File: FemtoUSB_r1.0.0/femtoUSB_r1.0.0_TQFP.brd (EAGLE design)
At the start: 20.7 x 15.2 mm, 25 parts, among them IC1 ATSAMD21E18A-AU

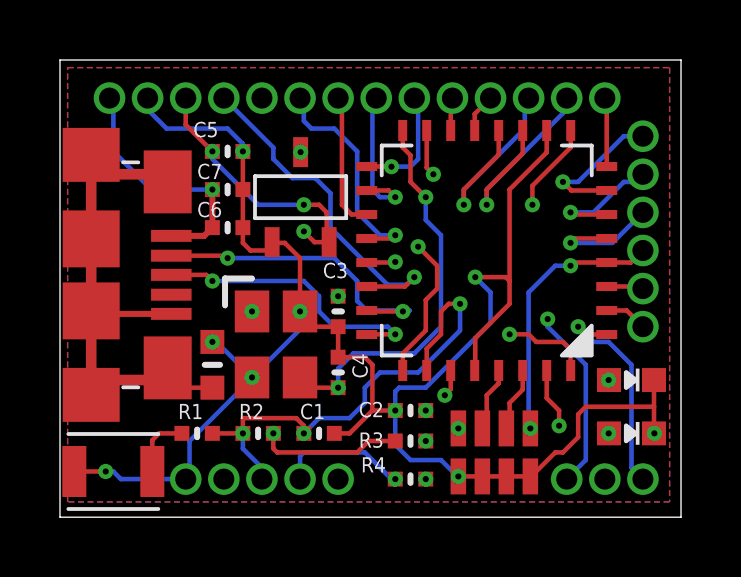
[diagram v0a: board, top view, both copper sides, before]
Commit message: Corrected the Make and model of the LDO Voltage Regulator. Board now powers on.
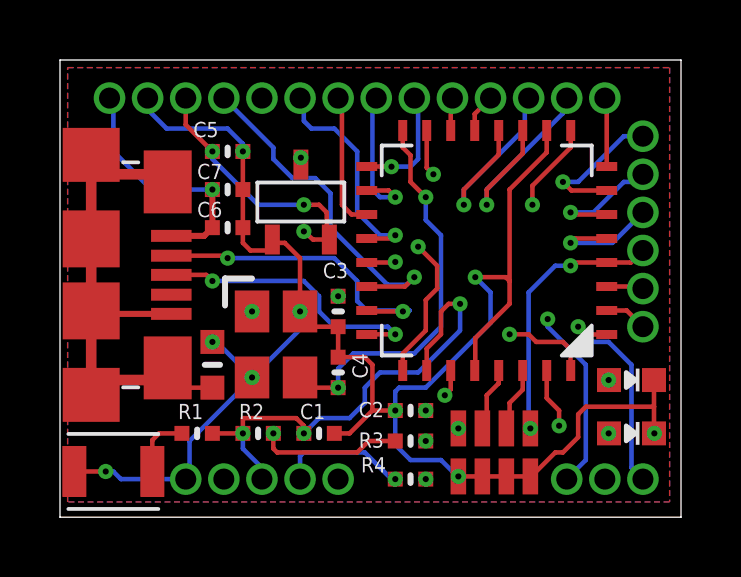
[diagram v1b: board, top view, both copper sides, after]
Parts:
- LDO_VREG: value LM3480 -> MCP1700T-3302E/TT; device ti-lm3480:LM3480 -> MCP1700T-3302E_TT:MCP1700T-3302E/TT
- moved LDO_VREG 1.64 mm to (6.58, 9.86)
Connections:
- net 3.3V: now also LDO_VREG.VOUT; no longer LDO_VREG.P$2
- net GND: now also LDO_VREG.GND; no longer LDO_VREG.P$1
- net VIN: now also LDO_VREG.VIN; no longer LDO_VREG.P$3
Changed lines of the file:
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@@
 <setting verticaltext="up"/>
 </settings>
-<grid distance="10" unitdist="mil" unit="mil" style="lines" multiple="1" display="no" altdistance="0.025" altunitdist="inch" altunit="inch"/>
+<grid distance="1" unitdist="mil" unit="mil" style="lines" multiple="1" display="no" altdistance="0.025" altunitdist="inch" altunit="inch"/>
 <layers>
 <layer number="1" name="Top" color="4" fill="1" visible="yes" active="yes"/>
@@
 <attribute name="DIGIKEY_PART" value="TSX-3225 32.0000MF15X-B-ND" x="8.001" y="6.858" size="1.778" layer="27" rot="R270" display="off"/>
 </element>
-<element name="LDO_VREG" library="ti-lm3480" package="LM3480" value="LM3480" x="8.001" y="10.668"/>
+<element name="LDO_VREG" library="MCP1700T-3302E_TT" package="MCP1700T-3302E/TT" value="MCP1700T-3302E/TT" x="6.5786" y="9.8552"/>
 <element name="C5" library="microbuilder" package="_0402MP" value="2.2uF" x="5.588" y="12.192" smashed="yes">
 <attribute name="NAME" x="4.445" y="12.6683" size="0.508" layer="25" font="vector" ratio="20"/>
@@
 <contactref element="C4" pad="1"/>
 <contactref element="LED1" pad="C"/>
-<contactref element="LDO_VREG" pad="P$1"/>
+<contactref element="LDO_VREG" pad="GND"/>
 <contactref element="C5" pad="2"/>
 <contactref element="C6" pad="2"/>
@@
 <wire x1="8.001" y1="8.636" x2="7.493" y2="9.144" width="0.1524" layer="1"/>
 <wire x1="7.493" y1="9.144" x2="7.095" y2="9.144" width="0.1524" layer="1"/>
-<wire x1="7.095" y1="9.144" x2="7.071" y2="9.168" width="0.1524" layer="1"/>
+<wire x1="7.095" y1="9.144" x2="7.0786" y2="9.2552" width="0.1524" layer="1"/>
 <wire x1="2.921" y1="13.97" x2="2.921" y2="13.589" width="0.1524" layer="16"/>
 <wire x1="2.921" y1="13.589" x2="3.556" y2="12.954" width="0.1524" layer="16"/>
@@
 <wire x1="6.096" y1="9.144" x2="6.35" y2="8.89" width="0.1524" layer="1"/>
 <wire x1="6.35" y1="8.89" x2="7.047" y2="8.89" width="0.1524" layer="1"/>
-<wire x1="7.047" y1="8.89" x2="7.071" y2="9.168" width="0.1524" layer="1"/>
+<wire x1="7.047" y1="8.89" x2="7.0786" y2="9.2552" width="0.1524" layer="1"/>
 <wire x1="9.271" y1="6.35" x2="8.509" y2="6.35" width="0.1524" layer="1"/>
 <wire x1="8.509" y1="6.35" x2="8.001" y2="6.858" width="0.1524" layer="1"/>
@@
 <contactref element="C5" pad="1"/>
 <contactref element="R3" pad="1"/>
-<contactref element="LDO_VREG" pad="P$2"/>
+<contactref element="LDO_VREG" pad="VOUT"/>
 <via x="7.112" y="2.794" extent="1-16" drill="0.2032" diameter="0.508"/>
 <wire x1="7.112" y1="2.794" x2="6.477" y2="2.159" width="0.1524" layer="15"/>
@@
 <wire x1="8.636" y1="10.414" x2="8.89" y2="10.16" width="0.1524" layer="1"/>
 <wire x1="8.89" y1="10.16" x2="8.89" y2="9.249" width="0.1524" layer="1"/>
-<wire x1="8.89" y1="9.249" x2="8.971" y2="9.168" width="0.1524" layer="1"/>
+<wire x1="8.89" y1="9.249" x2="8.9786" y2="9.2552" width="0.1524" layer="1"/>
 <wire x1="6.604" y1="10.414" x2="8.128" y2="10.414" width="0.1524" layer="16"/>
-<wire x1="8.971" y1="9.168" x2="8.485" y2="9.168" width="0.1524" layer="1"/>
-<wire x1="8.485" y1="9.168" x2="8.128" y2="9.525" width="0.1524" layer="1"/>
+<wire x1="8.9786" y1="9.2552" x2="8.4342" y2="9.2552" width="0.1524" layer="1"/>
+<wire x1="8.4342" y1="9.2552" x2="8.128" y2="9.525" width="0.1524" layer="1"/>
 <via x="8.128" y="9.525" extent="1-16" drill="0.2032" diameter="0.508"/>
 <wire x1="8.128" y1="9.525" x2="7.874" y2="9.525" width="0.1524" layer="15"/>
@@
 <signal name="VIN">
 <contactref element="U$6" pad="P$1"/>
-<contactref element="LDO_VREG" pad="P$3"/>
+<contactref element="LDO_VREG" pad="VIN"/>
 <contactref element="C6" pad="1"/>
 <contactref element="C7" pad="1"/>
@@
 <wire x1="1.778" y1="13.843" x2="1.651" y2="13.97" width="0.1524" layer="16"/>
 <wire x1="5.08" y1="10.922" x2="7.62" y2="10.922" width="0.254" layer="15"/>
-<wire x1="7.62" y1="10.922" x2="8.021" y2="11.323" width="0.254" layer="15"/>
-<via x="8.021" y="12.168" extent="1-16" drill="0.2032" diameter="0.508"/>
-<wire x1="8.021" y1="12.168" x2="8.021" y2="11.323" width="0.254" layer="15"/>
+<wire x1="7.62" y1="10.922" x2="8.0286" y2="11.323" width="0.254" layer="15"/>
+<via x="8.0286" y="11.9838" extent="1-16" drill="0.2032" diameter="0.508"/>
+<wire x1="8.0286" y1="11.9838" x2="8.0286" y2="11.323" width="0.254" layer="15"/>
 </signal>
 <signal name="N$26">

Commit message: Corrected the snubbing circuits by adding the missing 10uH inductor, and two missing 10uF capacitors. Also corrected the connection from VDDIN pin to 3V3
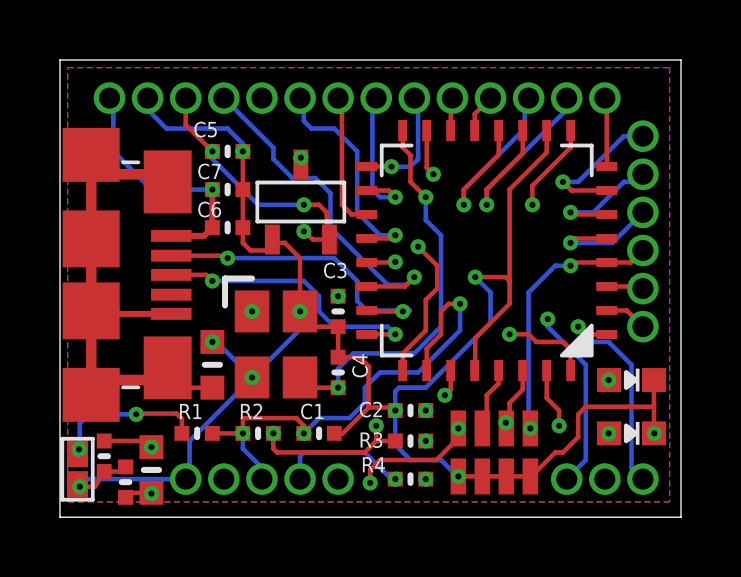
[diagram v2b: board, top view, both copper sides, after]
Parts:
- added C8, C9: 10uF, microbuilder:_0402MP
- added L1: 10uH, microbuilder:_0603MP
- BTN: device omron_tactile_switch:SIDE_ACT_NO_GND_NO_BOSS -> femtoduino:SPST_SMD
- moved BTN 1.20 mm to (0.58, 1.60), turned to 270 degrees
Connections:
- removed net VDDIN: C_ARR1.5, IC1.30
- net 3.3V: now also C8.2, C_ARR1.5, IC1.30, L1.1
- net GND: now also C8.1, C9.1
- net VDDANA: now also C9.2, L1.2
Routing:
- net VDDANA: track 15.9 -> 29.7 mm, vias 2 -> 4
- net 3.3V: track 25.7 -> 38.8 mm, vias 4 -> 7
- net N$26: track 2.12 -> 5.12 mm, vias 0 -> 2
- net VDDIN: track 2.14 -> 0.00 mm
- net GND: track 62.5 -> 64.2 mm
- net N$1: track 11.4 -> 11.9 mm

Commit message: Updating r1.x version of FemtoUSB (QFN and QFP chip version). Pin PA15 and GND pads now available to start board up in bootloader mode (SAM-BA)
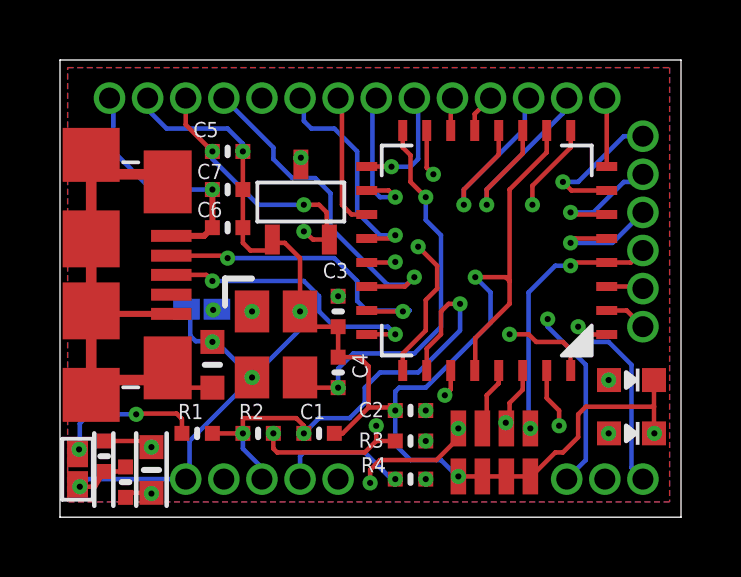
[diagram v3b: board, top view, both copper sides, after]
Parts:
- added U$38: SPST_SMD, femtoduino:SPST_SMD
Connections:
- net GND: now also U$38.2
- net PA15/XOUT: now also U$38.1
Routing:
- net PA15/XOUT: track 13.1 -> 18.5 mm, vias 2 -> 3
- net GND: track 64.2 -> 66.0 mm
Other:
- board text added: "r1.0.2 TQFP"
- board text removed: "r1.0.0 TQFP"
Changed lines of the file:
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@@
 <setting verticaltext="up"/>
 </settings>
-<grid distance="1" unitdist="mil" unit="mil" style="lines" multiple="1" display="no" altdistance="0.025" altunitdist="inch" altunit="inch"/>
+<grid distance="5" unitdist="mil" unit="mil" style="lines" multiple="1" display="no" altdistance="0.025" altunitdist="inch" altunit="inch"/>
 <layers>
 <layer number="1" name="Top" color="4" fill="1" visible="yes" active="yes"/>
@@
 <wire x1="20.701" y1="15.24" x2="0" y2="15.24" width="0" layer="20"/>
 <wire x1="0" y1="15.24" x2="0" y2="0" width="0" layer="20"/>
-<text x="3.429" y="4.572" size="0.7112" layer="26" font="vector" ratio="20" rot="MR90">FemtoUSB</text>
-<text x="2.159" y="4.445" size="0.7112" layer="26" font="vector" ratio="20" rot="MR90">r1.0.0 TQFP</text>
+<text x="3.048" y="4.0386" size="0.7112" layer="26" font="vector" ratio="20" rot="MR90">FemtoUSB</text>
+<text x="1.6002" y="4.0132" size="0.7112" layer="26" font="vector" ratio="20" rot="MR90">r1.0.2 TQFP</text>
 <text x="0.762" y="3.175" size="0.7112" layer="26" font="vector" ratio="20" rot="MR90">femtoduino.com</text>
 <text x="2.032" y="13.081" size="0.7112" layer="26" font="vector" ratio="20" rot="SMR90" align="top-right">VIN</text>
@@
 <circle x="16.2814" y="6.5786" radius="0.250159375" width="0.254" layer="26"/>
 <circle x="16.2814" y="5.5626" radius="0.250159375" width="0.254" layer="26"/>
+<polygon width="0.1524" layer="26">
+<vertex x="5.715" y="7.493"/>
+<vertex x="6.35" y="8.128"/>
+<vertex x="6.35" y="6.985"/>
+<vertex x="6.223" y="6.985"/>
+</polygon>
+<wire x1="2.54" y1="2.794" x2="2.54" y2="0.381" width="0.1524" layer="25"/>
+<wire x1="1.778" y1="2.794" x2="1.778" y2="0.381" width="0.1524" layer="25"/>
+<wire x1="1.143" y1="2.794" x2="1.143" y2="0.381" width="0.1524" layer="25"/>
+<wire x1="3.556" y1="2.794" x2="3.556" y2="0.381" width="0.1524" layer="25"/>
 </plain>
 <attributes>
@@
 <element name="C8" library="microbuilder" package="_0402MP" value="10uF" x="2.1844" y="1.1684" smashed="yes" rot="R270"/>
 <element name="C9" library="microbuilder" package="_0402MP" value="10uF" x="1.4732" y="2.032" smashed="yes" rot="R90"/>
+<element name="U$38" library="femtoduino" package="SPST_SMD" value="SPST_SMD" x="4.7244" y="6.9342" rot="MR0"/>
 </elements>
 <signals>
@@
 <wire x1="12.7" y1="9.398" x2="12.192" y2="9.906" width="0.1524" layer="16"/>
 <wire x1="12.192" y1="9.906" x2="12.192" y2="10.668" width="0.1524" layer="16"/>
+<contactref element="U$38" pad="1"/>
+<wire x1="5.2324" y1="6.9342" x2="5.207" y2="6.9088" width="0.1524" layer="16"/>
+<wire x1="5.207" y1="6.9088" x2="5.1054" y2="6.9088" width="0.1524" layer="16"/>
+<via x="5.1054" y="6.9088" extent="1-16" drill="0.2032" diameter="0.508"/>
+<wire x1="5.1054" y1="6.9088" x2="7.6962" y2="4.318" width="0.1524" layer="2"/>
+<wire x1="7.6962" y1="4.318" x2="9.271" y2="4.318" width="0.1524" layer="2"/>
 </signal>
 <signal name="PA16/SERCOM1/PAD[0]/SPI/I2C">
@@
 <wire x1="5.217" y1="5.842" x2="6.401" y2="4.658" width="0.1524" layer="16"/>
 <wire x1="6.401" y1="4.658" x2="6.401" y2="4.623" width="0.1524" layer="16"/>
-<wire x1="6.401" y1="4.623" x2="4.318" y2="2.54" width="0.1524" layer="16"/>
 <wire x1="4.318" y1="2.54" x2="4.318" y2="1.397" width="0.1524" layer="16"/>
 <wire x1="4.318" y1="1.397" x2="4.191" y2="1.27" width="0.1524" layer="16"/>
@@
 <wire x1="10.287" y1="3.6576" x2="11.176" y2="3.6576" width="0.1524" layer="1"/>
 <wire x1="11.176" y1="3.6576" x2="11.176" y2="3.556" width="0.1524" layer="1"/>
+<contactref element="U$38" pad="2"/>
+<wire x1="6.401" y1="4.623" x2="4.318" y2="2.54" width="0.1524" layer="16"/>
+<wire x1="4.3434" y1="6.0452" x2="4.5212" y2="5.8674" width="0.1524" layer="16"/>
+<wire x1="4.5212" y1="5.8674" x2="5.0546" y2="5.8674" width="0.1524" layer="16"/>
+<wire x1="5.0546" y1="5.8674" x2="5.08" y2="5.842" width="0.1524" layer="16"/>
+<wire x1="4.3434" y1="6.0452" x2="4.3434" y2="6.8072" width="0.1524" layer="16"/>
+<wire x1="4.3434" y1="6.8072" x2="4.2164" y2="6.9342" width="0.1524" layer="16"/>
 </signal>
 <signal name="3.3V">

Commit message: Updating gerbers and BoM/Partslist of QFN version
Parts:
- EPSON_TSX1: value 32MHz -> 48MHz
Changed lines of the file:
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@@
 </element>
 <element name="BTN" library="femtoduino" package="SPST_SMD" value="OMRON B3U-300P(M)" x="0.5842" y="1.6002" rot="R270"/>
-<element name="EPSON_TSX1" library="crystals" package="TSX-3225" value="32MHz" x="8.001" y="6.858" smashed="yes" rot="R270">
+<element name="EPSON_TSX1" library="crystals" package="TSX-3225" value="48MHz" x="8.001" y="6.858" smashed="yes" rot="R270">
 <attribute name="DIGIKEY_PART" value="TSX-3225 32.0000MF15X-B-ND" x="8.001" y="6.858" size="1.778" layer="27" rot="R270" display="off"/>
 </element>
